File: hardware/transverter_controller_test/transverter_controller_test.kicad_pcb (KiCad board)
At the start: 2 copper layers, 50 x 50 mm, 43 parts, among them J1 CNC Tech 3020-10-0200-00‎, J2 USB_C_Receptacle_USB2.0, J3 Conn_01x03_Male, J4 CNC Tech 3020-10-0200-00‎, M1 Logo_10mmx10mm, Q1 DMN62D0U-13, Q2 DMN62D0U-13, U1 PCT2075D, U2 24LC024-I/SN, U3 MKL26Z64VFT4, U4 MAX3483ESA+, Y1 830108178109

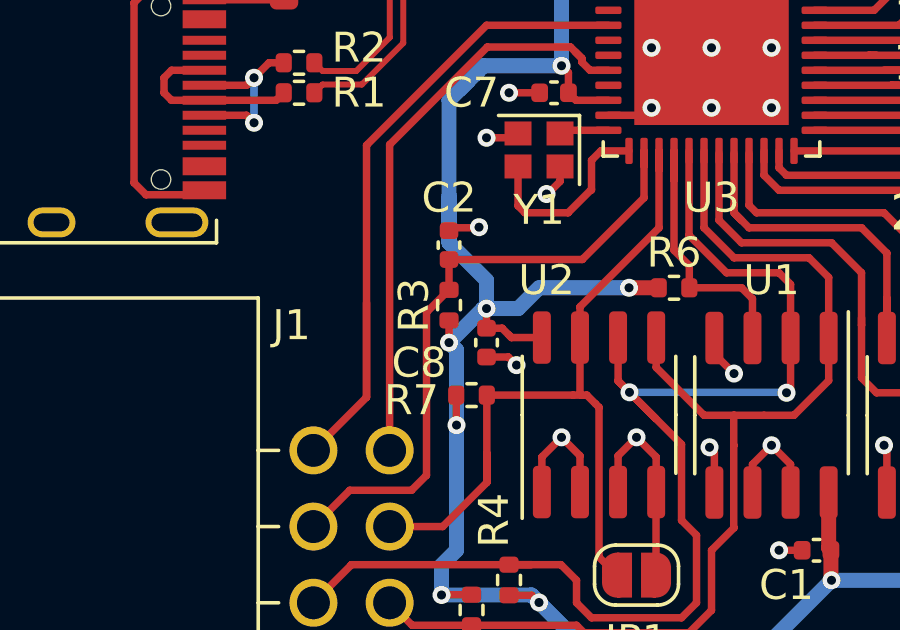
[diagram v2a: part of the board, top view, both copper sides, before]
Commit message: Added RS485 driver and AXI GPIO for read/write
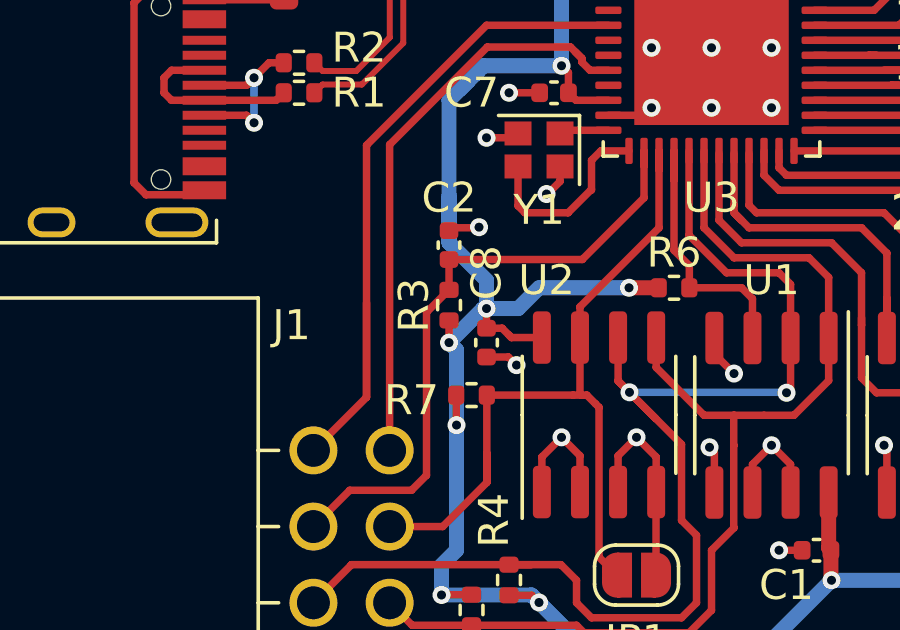
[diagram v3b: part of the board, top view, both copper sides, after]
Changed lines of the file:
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@@
     (property "Sheetname" "")
     (attr smd)
-    (fp_text reference "C8" (at 0.671875 2.25 180) (layer "F.SilkS")
+    (fp_text reference "C8" (at -2.328125 0 -90) (layer "F.SilkS")
       (effects (font (size 1 1) (thickness 0.15)))
     )

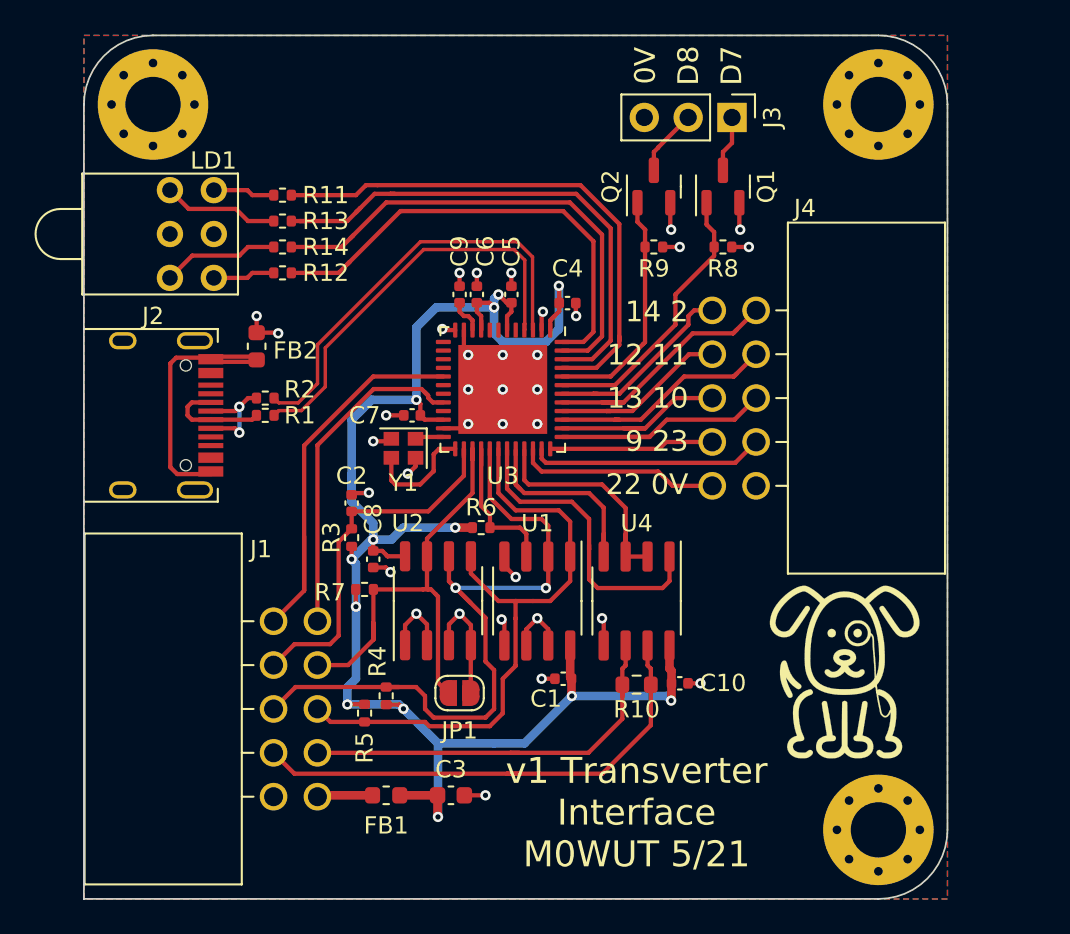
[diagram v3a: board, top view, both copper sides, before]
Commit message: Added RS485 test board
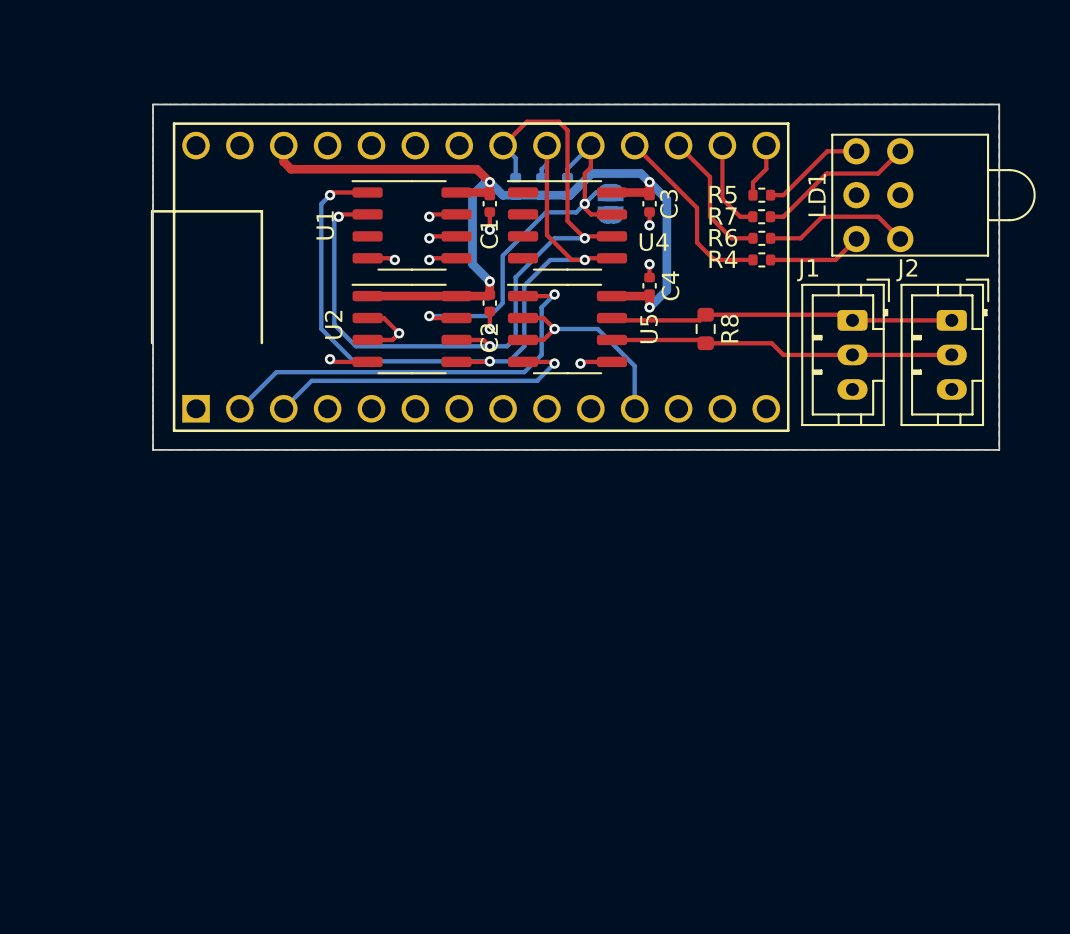
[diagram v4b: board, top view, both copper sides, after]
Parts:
- removed C10, C5, C6, C7, C8, C9: 100n, Capacitor_SMD:C_0402_1005Metric
- removed FB1, FB2: FerriteBead_Small, Inductor_SMD:L_0603_1608Metric
- removed H1, H2, H3: MountingHole_Pad, MountingHole:MountingHole_3.2mm_M3_Pad_Via
- removed J3: Conn_01x03_Male, Connector_PinHeader_2.54mm:PinHeader_1x03_P2.54mm_Vertical
- removed J4: CNC Tech 3020-10-0200-00‎, Connector_WUT:Header_CNC-Tech_3020-10-0200-00_2x5_TH_RA
- removed Q1, Q2: DMN62D0U-13, Package_TO_SOT_SMD:SOT-23
- removed R10: DNF, Resistor_SMD:R_0603_1608Metric
- removed R11, R12, R13, R14: 1k, Resistor_SMD:R_0402_1005Metric
- removed R9: 10k, Resistor_SMD:R_0402_1005Metric
- removed Y1: 830108178109, Crystal:Crystal_SMD_2016-4Pin_2.0x1.6mm
- added U5: MAX3483ESA+, Package_SO:SO-8_3.9x4.9mm_P1.27mm, F.Cu at (123.0, 74.0)
- C2: value DNF -> 100n
- C3: value 10u -> 100n; footprint Capacitor_SMD:C_0603_1608Metric -> Capacitor_SMD:C_0402_1005Metric
- J1: value CNC Tech 3020-10-0200-00‎ -> Conn_01x03_Male; footprint Connector_WUT:Header_CNC-Tech_3020-10-0200-00_2x5_TH_RA -> Connector_JST:JST_PH_B3B-PH-K_1x03_P2.00mm_Vertical
- J2: value USB_C_Receptacle_USB2.0 -> Conn_01x03_Male; footprint Connector_WUT:USB-C_HRO_TYPE-C-31-M-12 -> Connector_JST:JST_PH_B3B-PH-K_1x03_P2.00mm_Vertical
- JP1, M1: moved to B.Cu
- R1, R2: value 33 -> 4k7; moved to B.Cu
- R3: value 10k -> 1k; moved to B.Cu
- R4, R5: value 4k7 -> 1k
- R6: value 10k -> 1k
- R8: value 10k -> DNF; footprint Resistor_SMD:R_0402_1005Metric -> Resistor_SMD:R_0603_1608Metric
- U3: value MKL26Z64VFT4 -> Teensy-LC; footprint Package_DFN_QFN:QFN-48-1EP_7x7mm_P0.5mm_EP5.15x5.15mm -> teensy:Teensy_LC
- U4: value MAX3483ESA+ -> 24LC024-I/SN
- moved J2 48.3 mm to (145.2, 73.5)
- moved M1 41.7 mm to (104.2, 71.0), turned to 180 degrees
- moved J1 38.3 mm to (139.5, 73.5)
- moved R5 37.8 mm to (134.2, 66.2), turned to 0 degrees
- moved LD1 37.3 mm to (139.7, 66.2), turned to 90 degrees
- moved C3 36.1 mm to (127.8, 66.8), turned to -90 degrees
- moved R4 33.3 mm to (134.2, 70.0), turned to 0 degrees
- moved R7 31.5 mm to (134.2, 67.5)
- moved JP1 29.6 mm to (125.5, 66.8), turned to -90 degrees
- moved C1 27.8 mm to (118.5, 66.8), turned to -90 degrees
- moved R3 23.9 mm to (123.0, 65.8)
- moved R6 23.3 mm to (134.2, 68.8)
- moved U1 22.9 mm to (114.0, 68.0), turned to 0 degrees
- moved U4 22.1 mm to (123.0, 68.0), turned to 0 degrees
- moved R2 20.2 mm to (121.5, 65.8), turned to 90 degrees
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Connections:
- C2 pad 1: /RESET_B -> +3V3
- J1 pad 1: Net-(FB1-Pad2) -> Net-(J1-Pad1)
- J1 pad 2: GND -> Net-(J1-Pad2)
- J1 pad 3: /RS485_A -> GND
- R1 pad 1: Net-(J2-PadA7) -> +3V3
- R1 pad 2: /D_P -> /SCL
- R2 pad 1: Net-(J2-PadA6) -> +3V3
- R2 pad 2: /D_N -> /SDA
- R3 pad 2: /RESET_B -> /WP
- R4 pad 1: +3V3 -> /LED_TX
- R4 pad 2: /SCL -> Net-(LD1-Pad1)
- R5 pad 1: +3V3 -> /LED_RX
- R5 pad 2: /SDA -> Net-(LD1-Pad3)
- R6 pad 1: +3V3 -> /LED_ERROR
- R6 pad 2: /~OVERTEMP -> Net-(LD1-Pad4)
- R7 pad 1: +3V3 -> /LED_STATUS
- R7 pad 2: /WP -> Net-(LD1-Pad6)
- R8 pad 1: Net-(Q1-Pad1) -> Net-(J1-Pad1)
- R8 pad 2: GND -> Net-(J1-Pad2)
- U1 pad 3: /~OVERTEMP -> unconnected-(U1-Pad3)
- U2 pad 1: GND -> +3V3
- U3 pad 1: +3V3 -> GND
- U3 pad 10: Net-(C9-Pad1) -> unconnected-(U3-Pad10)
- U3 pad 11: GND -> /~R~/W
- U3 pad 12: GND -> unconnected-(U3-Pad12)
- U3 pad 2: GND -> /RX
- U3 pad 20: /PTA3 -> /LED_RX
- U3 pad 21: unconnected-(U3-Pad21) -> /LED_STATUS
- U3 pad 22: +3V3 -> /LED_ERROR
- U3 pad 23: GND -> /LED_TX
- U3 pad 24: Net-(U3-Pad24) -> /WP
- U3 pad 25: Net-(U3-Pad25) -> /SDA
- U3 pad 26: /RESET_B -> /SCL
- U3 pad 27: /WP -> unconnected-(U3-Pad27)
- U3 pad 28: /~OVERTEMP -> unconnected-(U3-Pad28)
- U3 pad 29: /SCL -> unconnected-(U3-Pad29)
- U3 pad 3: /D_N -> /TX
- U3 pad 30: /SDA -> unconnected-(U3-Pad30)
- U3 pad 31: /RX -> +3V3
- U3 pad 32: /TX -> GND
- U3 pad 33: /~R~/W -> unconnected-(U3-Pad33)
- U3 pad 4: /D_P -> unconnected-(U3-Pad4)
- U3 pad 6: +3V3 -> unconnected-(U3-Pad6)
- U3 pad 9: +3V3 -> unconnected-(U3-Pad9)
- U4 pad 1: /RX -> GND
- U4 pad 2: /~R~/W -> GND
- U4 pad 3: /~R~/W -> GND
- U4 pad 4: /TX -> GND
- U4 pad 5: GND -> /SDA
- U4 pad 6: /RS485_A -> /SCL
- U4 pad 7: /RS485_B -> /WP
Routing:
- net +3V3: track 101.7 -> 55.0 mm, vias 13 -> 4
- net /RS485_B: track 29.0 -> 0.00 mm
- net GND: track 45.8 -> 18.3 mm, vias 35 -> 11
- net /D_N: track 24.9 -> 0.00 mm
- net /D_P: track 24.2 -> 0.00 mm
- net /LED_RX: track 27.2 -> 3.19 mm
- net /RS485_A: track 24.0 -> 0.00 mm
- net /PTA0: track 23.8 -> 0.00 mm
- net /LED_STATUS: track 28.6 -> 5.28 mm
- net /LED_ERROR: track 30.7 -> 7.88 mm
- net /RESET_B: track 21.4 -> 0.00 mm
- net /LED_TX: track 31.4 -> 10.8 mm
- net Net-(J1-Pad2): track 0.00 -> 20.0 mm
- net Net-(J1-Pad1): track 0.00 -> 19.8 mm
- net /PTA3: track 19.5 -> 0.00 mm
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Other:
- board size 50 x 50 mm -> 49 x 20 mm
- board text removed: "0V"
- board text removed: "12 11"
- board text removed: "13 10"
- board text removed: "14 2"
- board text removed: "22 0V"
- board text removed: "9 23"
- board text removed: "D7"
- board text removed: "D8"
- board text removed: "v1 Transverter Interface M0WUT 5/21"
